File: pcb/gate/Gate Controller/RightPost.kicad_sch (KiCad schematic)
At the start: 12 parts, among them J27 Conn_01x08_Female, J28 Pi, J29 Conn_01x08_Female, J30 Post, SW3 SW_Reed

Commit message: latest updates
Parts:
- J24: renamed from J28; footprint Connector_JST:JST_XH_PinSWAP -> Connector_JST:JST_XH_S8B-XH-A_1x08_P2.50mm_Horizontal
- J26: renamed from J30; footprint Connector_JST:JST_XH_PinSWAP -> Connector_JST:JST_XH_S8B-XH-A_1x08_P2.50mm_Horizontal
- renumbered J27 to J23, J29 to J25
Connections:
- net GND: no longer J23.2 (Pin_2), J24.2 (Pin_2), J26.2 (Pin_2)
- new net: J24.2 (Pin_2), J26.2 (Pin_2)
- new net GATE_LED_COM: J23.2 (Pin_2)

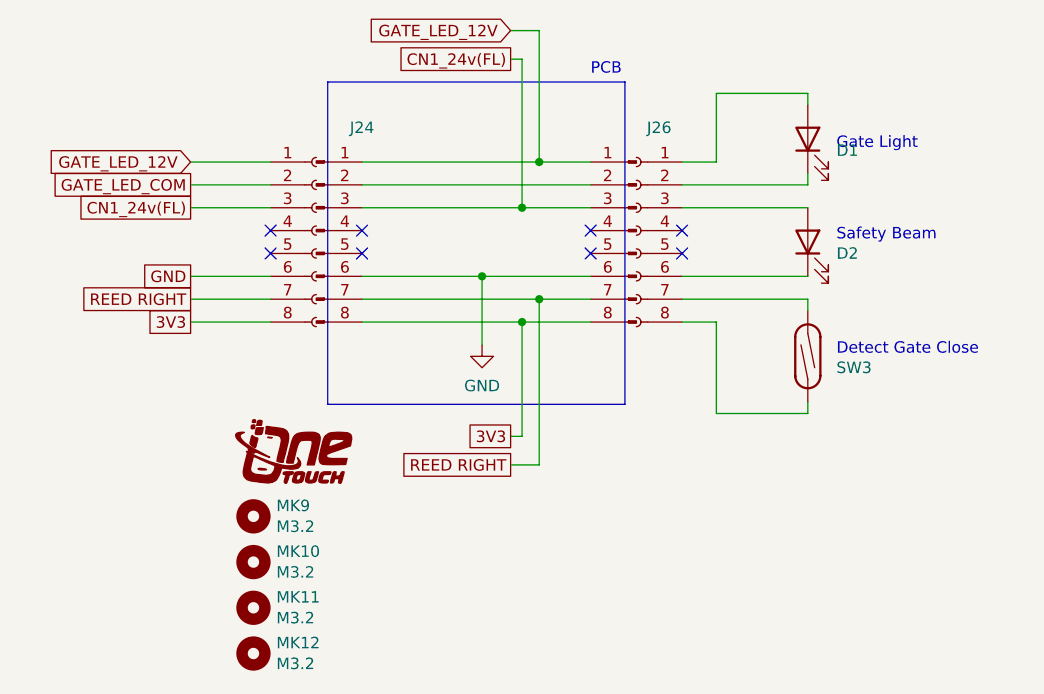
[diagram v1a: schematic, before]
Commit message: reworked to add i2c pullups and reduces unusedd components
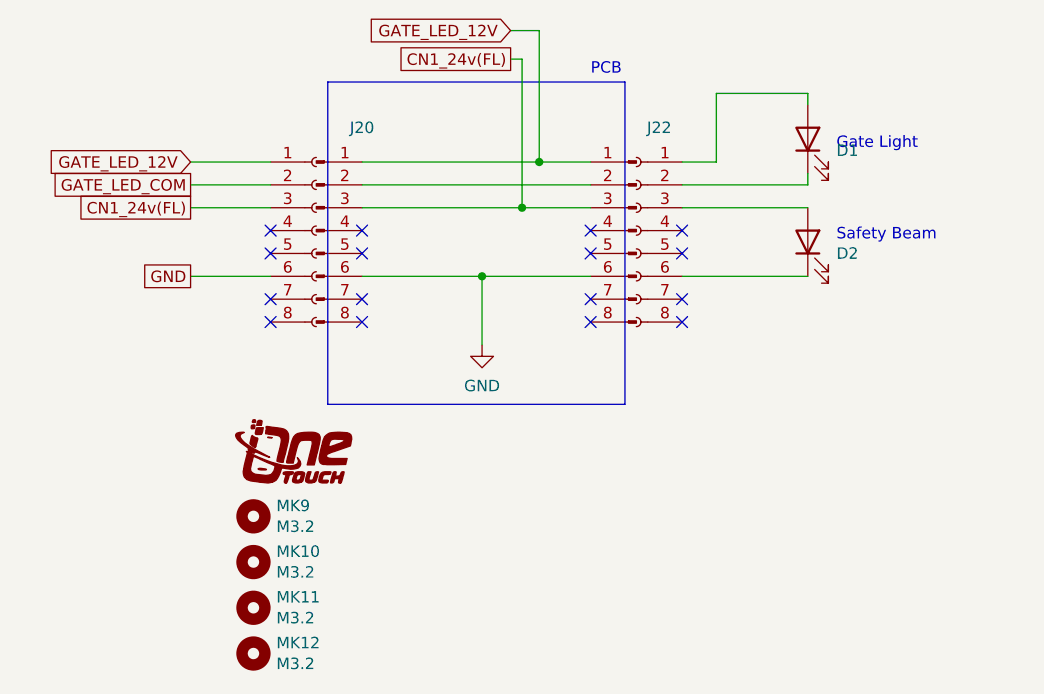
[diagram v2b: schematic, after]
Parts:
- removed SW3: SW_Reed, symbol Switch:SW_Reed
- renumbered J23 to J19, J24 to J20, J25 to J21, J26 to J22
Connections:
- removed net 3V3: J19.8 (Pin_8), J20.8 (Pin_8), J22.8 (Pin_8)
- removed net REED RIGHT: J19.7 (Pin_7), J20.7 (Pin_7), J22.7 (Pin_7)
- no-connect marks 8 -> 16
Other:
- note removed: "Detect Gate Close"
